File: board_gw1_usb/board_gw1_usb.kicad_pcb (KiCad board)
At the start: 4 copper layers, 50 x 15.2 mm, 212 parts, among them J1 USB_C_Receptacle, Q1 2N7002, Q10 2N7002, Q11 2N7002, Q12 2N7002, Q13 2N7002, Q14 2N7002, Q15 2N7002, Q16 2N7002, Q17 2N7002, Q18 2N7002, Q19 2N7002, Q2 2N7002, Q20 2N7002, Q21 2N7002, Q22 2N7002, Q23 2N7002, Q24 2N7002, Q25 2N7002, Q26 2N7002, Q27 2N7002, Q28 2N7002, Q29 2N7002, Q3 2N7002, Q30 2N7002, Q31 2N7002, Q32 2N7002, Q33 2N7002, Q34 2N7002, Q35 2N7002, Q36 2N7002, Q37 2N7002, Q38 2N7002, Q39 2N7002, Q4 2N7002, Q40 2N7002, Q41 2N7002, Q5 2N7002, Q6 2N7002, Q7 2N7002, Q8 2N7002, Q9 2N7002, U1 GW1NR-LV9-QN88-C6/I5, U11 FT232H, U2 ESD224DQA, U3 MIC5203-3.3BM5, U4 APS6404L-3SQR-ZR, U5 MIC5504-1.2YM5, U6 AP62150Z6, U7 W25Q16JVUXIQ, X1 27MHz

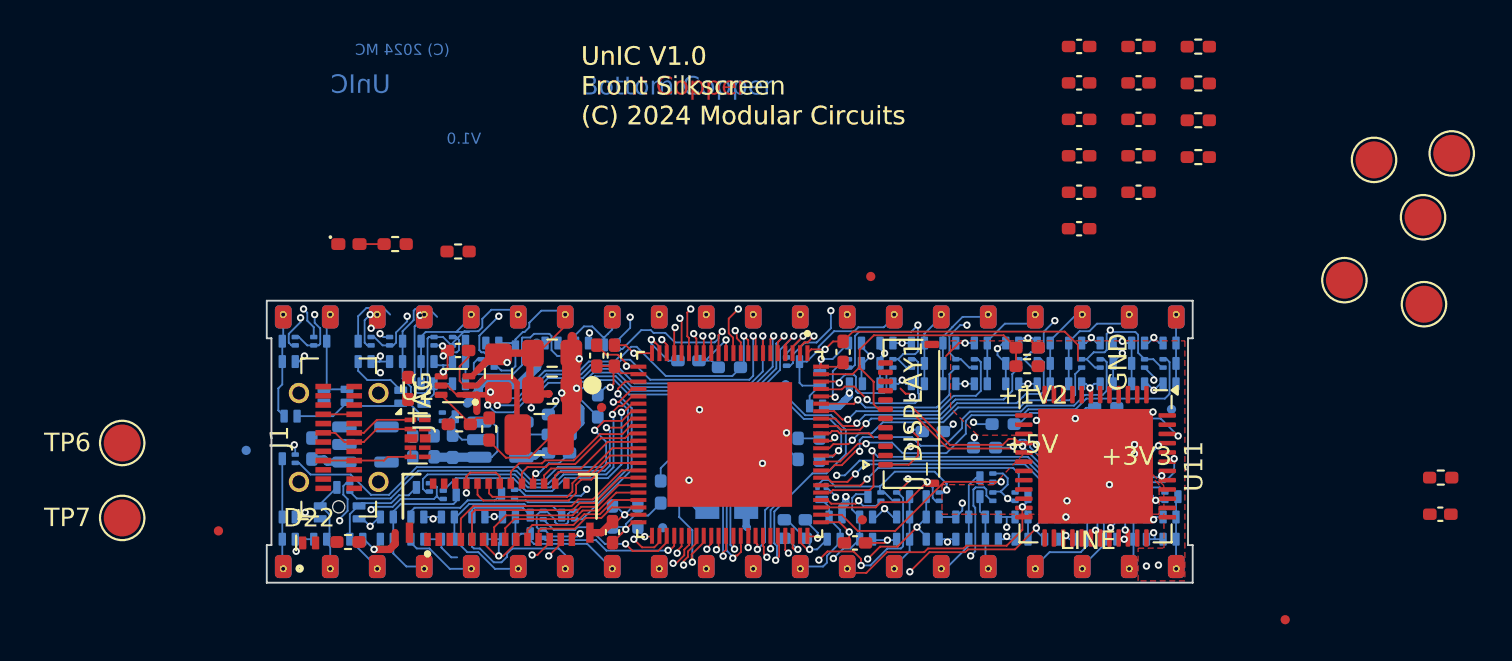
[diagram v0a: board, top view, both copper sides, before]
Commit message: Integrated JTAG controller mostly routed.
There are still some keepout violations and power nets
are incomplete, but at least there's a light at the end
if the tunnel.
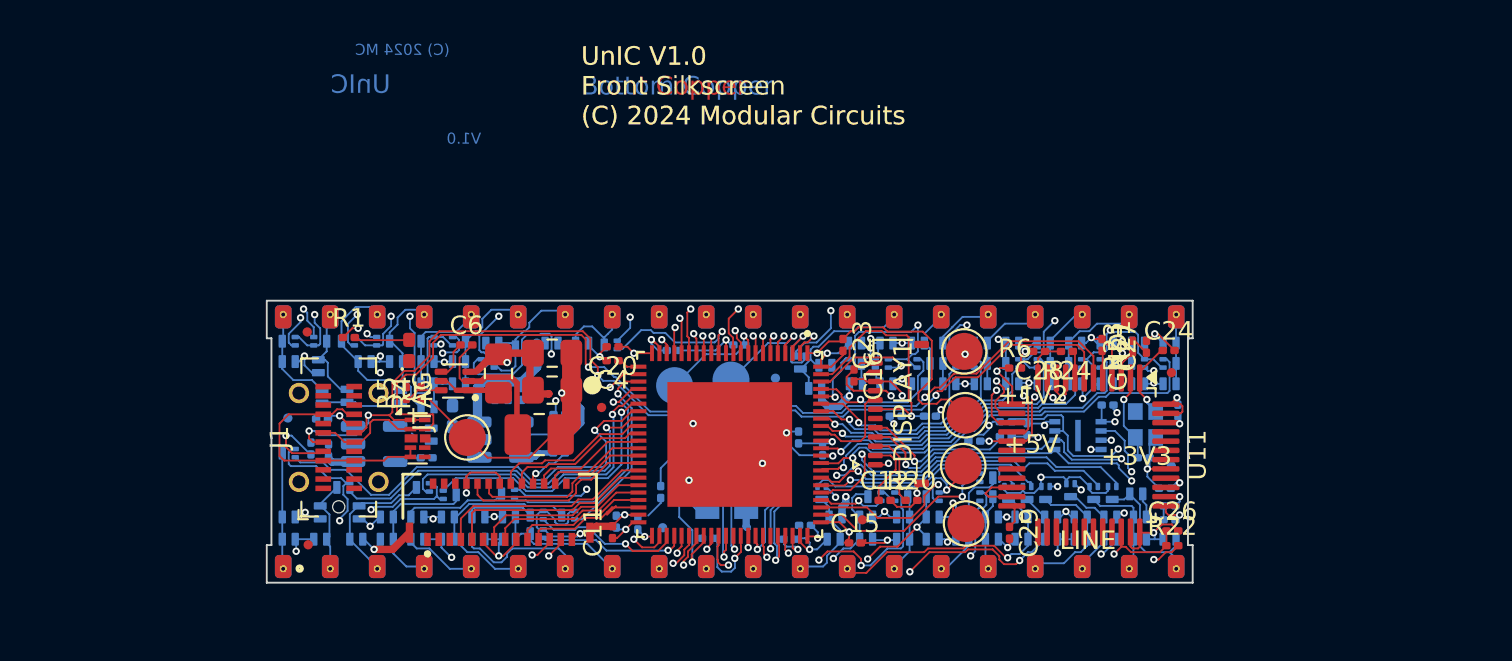
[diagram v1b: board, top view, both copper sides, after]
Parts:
- removed C32: 2.2u, UNIC:C_0402_1005Metric_Pad0.74x0.62mm_HandSolder
- added Y1: 12MHz, Crystal:Crystal_SMD_2016-4Pin_2.0x1.6mm, B.Cu at (85.8, 61.8)
- C1: footprint UNIC:C_0402_1005Metric_Pad0.74x0.62mm_HandSolder -> Capacitor_SMD:C_0402_1005Metric_Pad0.74x0.62mm_HandSolder
- C10, C11, C12, C13, C14, C15, C17, C18, C19, C2, C20, C21, C22, C23, C24, C26, C27, C28, C29, C3, C4, C6, C9: footprint UNIC:C_0402_1005Metric_Pad0.74x0.62mm_HandSolder -> Capacitor_SMD:C_0201_0603Metric
- C16: footprint UNIC:C_0402_1005Metric_Pad0.74x0.62mm_HandSolder -> Capacitor_SMD:C_0201_0603Metric; moved to F.Cu
- C25, C30, C31, C33, C34: footprint UNIC:C_0402_1005Metric_Pad0.74x0.62mm_HandSolder -> Capacitor_SMD:C_0201_0603Metric; moved to B.Cu
- D22, TP6, TP7: moved to B.Cu
- R1, R10, R11, R12, R13, R14, R15, R17, R20, R21, R22, R23, R24, R4, R5, R7, R8, R9: footprint UNIC:R_0402_1005Metric_Pad0.72x0.64mm_HandSolder -> Resistor_SMD:R_0201_0603Metric
- R16, R18, R19, R2, R3: footprint UNIC:R_0402_1005Metric_Pad0.72x0.64mm_HandSolder -> Resistor_SMD:R_0201_0603Metric; moved to B.Cu
- R6: footprint UNIC:R_0402_1005Metric_Pad0.72x0.64mm_HandSolder -> Resistor_SMD:R_0201_0603Metric; moved to F.Cu
- U11: footprint Package_DFN_QFN:QFN-48-1EP_8x8mm_P0.5mm_EP6.2x6.2mm -> Package_QFP:LQFP-48_7x7mm_P0.5mm
- moved TP3 53.0 mm to (49.1, 62.5)
- moved FID2 33.7 mm to (40.5, 68.3)
- moved TP6 33.1 mm to (63.4, 59.4), turned to 180 degrees
- moved TP7 30.7 mm to (60.3, 59.7), turned to 180 degrees
- moved C12 30.0 mm to (71.7, 65.9)
- moved R16 29.7 mm to (76.5, 62.7)
- moved R20 28.6 mm to (73.1, 65.9)
- moved TP5 28.4 mm to (76.0, 57.8)
- moved TP1 27.4 mm to (76.1, 67.1)
- moved TP4 26.1 mm to (76.0, 61.3)
- moved R22 25.0 mm to (87.2, 68.3)
- moved TP2 22.9 mm to (75.9, 64.0)
- moved C26 22.8 mm to (87.2, 67.5)
- moved R6 22.6 mm to (78.7, 58.7), turned to 0 degrees
- moved C31 22.0 mm to (86.8, 65.2), turned to 180 degrees
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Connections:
- J_EXT1 pad 1: /JTAG_SEL_N -> unconnected-(J_EXT1-Pin_1-Pad1)
- J_EXT1 pad 2: /JTAG_TDI -> unconnected-(J_EXT1-Pin_2-Pad2)
- J_EXT1 pad 3: /RECONFIG_N -> unconnected-(J_EXT1-Pin_3-Pad3)
- J_EXT1 pad 4: /JTAG_TDO -> unconnected-(J_EXT1-Pin_4-Pad4)
- J_EXT1 pad 5: /JTAG_TMS -> unconnected-(J_EXT1-Pin_5-Pad5)
- J_EXT1 pad 6: /JTAG_TCK -> unconnected-(J_EXT1-Pin_6-Pad6)
- U11 pad 18: /RECONFIG_N -> unconnected-(U11-ADBUS5-Pad18)
- U11 pad 19: /DONE -> unconnected-(U11-ADBUS6-Pad19)
- U2 pad 10: unconnected-(U2-Pad10) -> /USB_DP
- U2 pad 9: unconnected-(U2-Pad9) -> /USB_DM
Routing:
- net /USB_DP: track 3.33 -> 57.0 mm, vias 0 -> 4
- net /USB_DM: track 5.21 -> 56.5 mm, vias 0 -> 2
- net GND: track 85.7 -> 112.3 mm, vias 40 -> 44
- net /RECONFIG_N: track 18.5 -> 6.28 mm, vias 2 -> 1
- net /JTAG_SEL_N: track 14.1 -> 26.2 mm, vias 2 -> 3
- net +3V3: track 48.8 -> 60.1 mm, vias 15 -> 17
- net /SPI_MISO_IO1: track 53.5 -> 44.0 mm
- net /SPI_IO3: track 49.7 -> 40.8 mm
- net /SPI_MOSI_IO0: track 55.2 -> 47.8 mm
- net /VBUS: track 6.96 -> 14.0 mm
- net /SPI_IO2: track 47.1 -> 40.2 mm
- net +5V: track 93.2 -> 99.6 mm, vias 21 -> 17
- net /FLASH_CS_N: track 36.5 -> 30.3 mm
- net LINE: track 48.7 -> 42.8 mm
- net /SPI_CLK: track 53.9 -> 48.5 mm
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- removed copper zone on F.Cu, net +3V3
- removed copper zone on F.Cu, net +5V

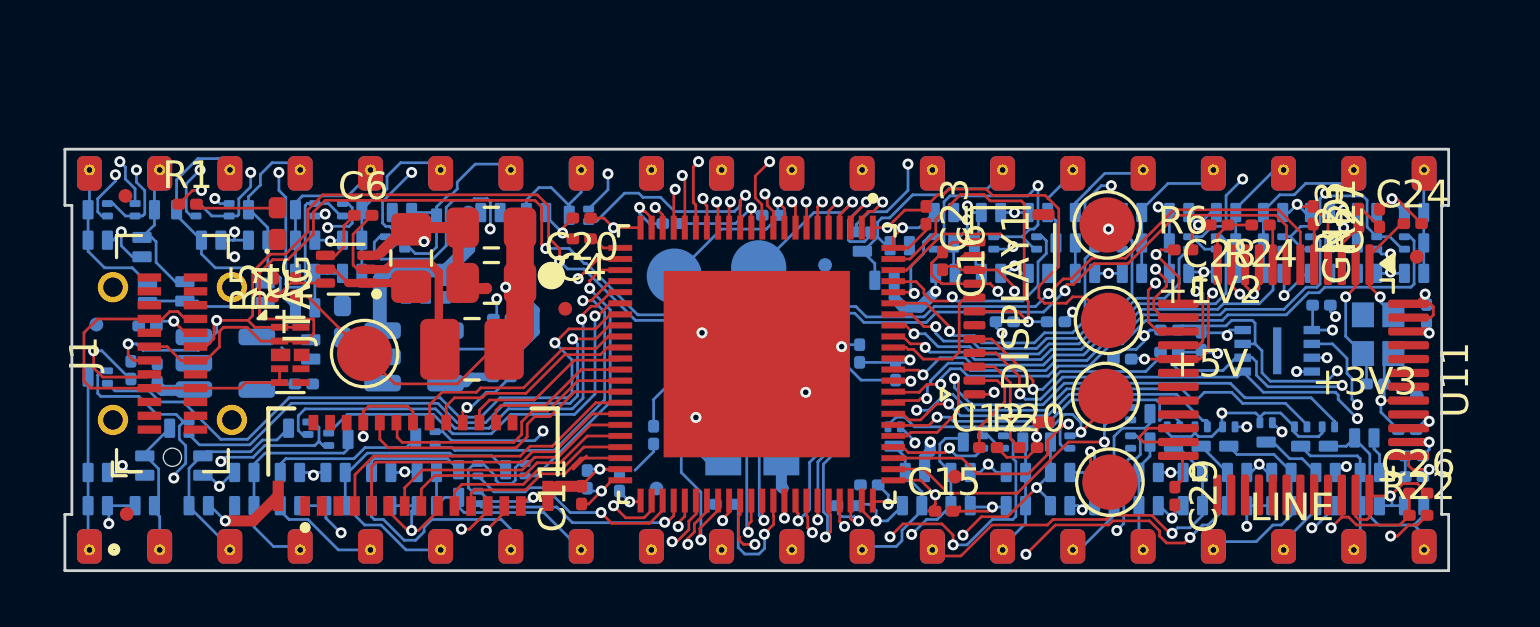
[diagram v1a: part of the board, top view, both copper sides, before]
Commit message: UnIC with FT232H is fully routed.
Not all that nicely, power needs a lot more work. But at least
connectivity is there.
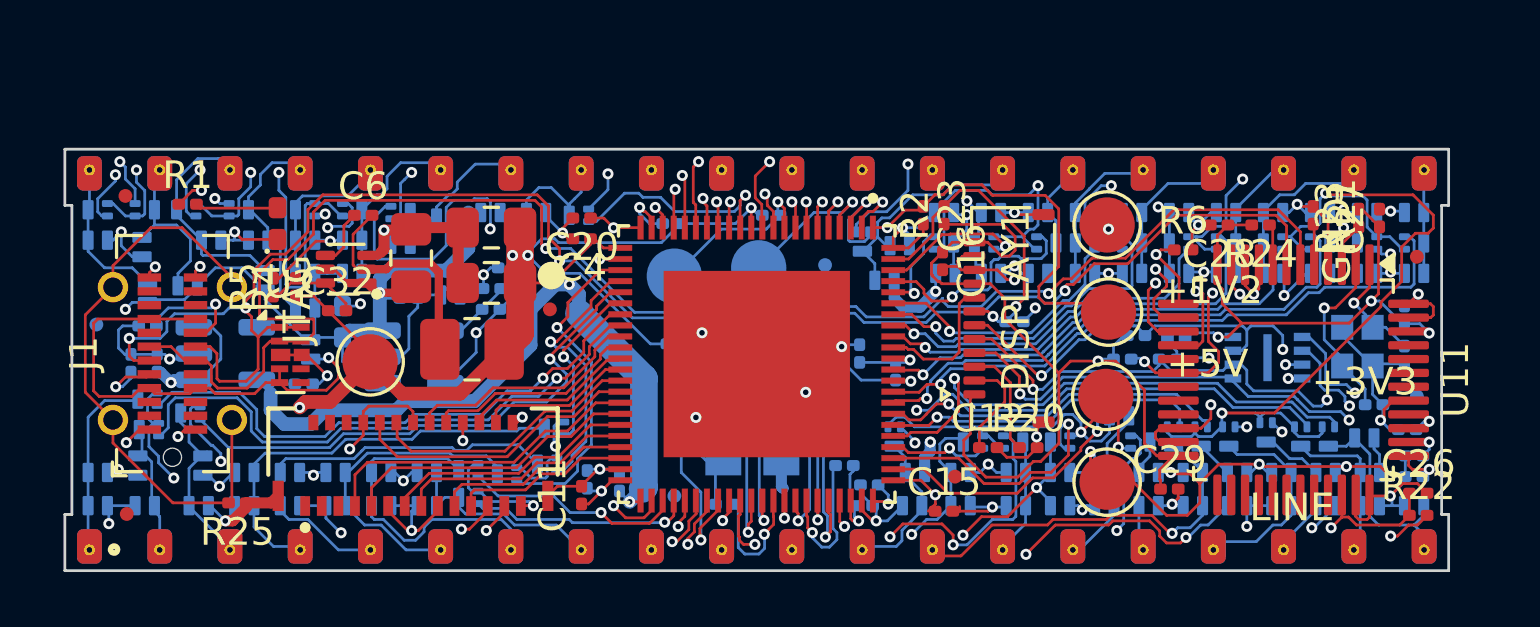
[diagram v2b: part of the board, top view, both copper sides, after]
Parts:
- added C32: 33p, Capacitor_SMD:C_0201_0603Metric, F.Cu at (48.1, 60.9)
- added R25: 0, Resistor_SMD:R_0201_0603Metric, F.Cu at (44.5, 67.9)
- C24: moved to B.Cu
- R2: moved to F.Cu
- U6: value AP62150Z6 -> TPS562242
- Y1: footprint Crystal:Crystal_SMD_2016-4Pin_2.0x1.6mm -> UNIC:Crystal_SMD_2016-4Pin_2.0x1.6mm
- moved R8 18.2 mm to (66.5, 66.5)
- moved Q2 7.81 mm to (56.0, 65.2), turned to 180 degrees
- moved C24 4.76 mm to (86.7, 62.5), turned to -90 degrees
- moved Q8 4.50 mm to (55.7, 66.5)
- moved R2 4.43 mm to (70.1, 57.5), turned to 90 degrees
- moved C3 3.94 mm to (54.3, 59.4), turned to 180 degrees
- moved Q3 3.94 mm to (42.8, 64.6)
- moved R9 3.40 mm to (60.4, 62.1), turned to 0 degrees
- moved Q1 1.97 mm to (41.3, 64.1)
- moved R3 1.50 mm to (72.6, 61.3)
- moved R14 1.49 mm to (53.7, 60.9)
- moved R17 1.39 mm to (50.7, 60.5), turned to 0 degrees
- moved Q41 1.25 mm to (52.2, 60.4), turned to 180 degrees
- moved R10 1.22 mm to (77.0, 61.8)
- moved R15 1.17 mm to (53.7, 60.1)
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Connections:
- J1 pad S1: GND -> Net-(J1-SHIELD)
- J_DISPLAY1 pad 6: /SPI_IO2 -> /SPI_IO3
- U11 pad 17: /JTAG_SEL_N -> unconnected-(U11-ADBUS4-Pad17)
- U11 pad 18: unconnected-(U11-ADBUS5-Pad18) -> /JTAG_SEL_N
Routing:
- net +3V3: track 60.1 -> 201.1 mm, vias 17 -> 18
- net LINE: track 42.8 -> 154.8 mm, vias 17 -> 19
- net +5V: track 99.6 -> 197.6 mm, vias 17 -> 18
- net +1V2: track 40.7 -> 67.8 mm, vias 4 -> 5
- net Net-(J1-SHIELD): track 0.00 -> 22.4 mm
- net GND: track 112.3 -> 128.8 mm, vias 44 -> 52
- net /SPI_IO3: track 40.8 -> 49.4 mm, vias 2 -> 3
- net /PIN4_F: track 14.7 -> 6.22 mm
- net /PIN4: track 8.21 -> 15.3 mm
- net Net-(Q41-D): track 0.00 -> 4.71 mm
- net /PIN5: track 10.8 -> 15.5 mm
- net /USB_DP: track 57.0 -> 61.1 mm
- net /VBUS: track 14.0 -> 18.0 mm, vias 0 -> 1
- net /PIN1_F: track 23.4 -> 19.7 mm
- net /FLASH_CS_N: track 30.3 -> 33.7 mm
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- removed copper zone on In2.Cu, net +1V2
- removed copper zone on In1.Cu, net +3V3
- removed copper zone on In2.Cu, net +3V3
- removed copper zone on In1.Cu, net +5V
- removed copper zone on In2.Cu, net +5V
- removed copper zone on In2.Cu, net LINE

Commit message: UnIC wuth ISB (V2.0) is pretty much complete.
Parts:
- C29: moved to B.Cu
- moved C29 3.24 mm to (78.7, 64.2)
- moved Q35 2.40 mm to (52.8, 57.3), turned to 180 degrees
- moved C3 2.16 mm to (54.1, 61.5), turned to 90 degrees
- moved D65 1.80 mm to (50.3, 57.6), turned to 90 degrees
- moved FID8 1.59 mm to (56.9, 59.7)
- moved D66 1.45 mm to (51.5, 57.6), turned to -90 degrees
- moved Q36 1.32 mm to (58.2, 57.3)
- moved D68 1.30 mm to (56.6, 57.4)
- moved D67 1.30 mm to (55.0, 57.4)
- moved FID6 0.91 mm to (87.3, 58.1)
- moved Q33 0.75 mm to (46.2, 57.3), turned to 0 degrees
- moved R14 0.72 mm to (53.4, 61.5), turned to 90 degrees
- moved Q13 0.63 mm to (75.8, 64.7), turned to 180 degrees
- moved C6 0.45 mm to (49.1, 57.9)
- moved R6 0.38 mm to (78.6, 58.4)
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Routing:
- net /PIN34_F: track 19.7 -> 11.1 mm
- net +5V: track 197.6 -> 191.0 mm, vias 18 -> 20
- net LINE: track 154.8 -> 148.4 mm, vias 19 -> 20
- net +3V3: track 201.1 -> 206.6 mm, vias 18 -> 19
- net /LCD_RST_N: track 11.5 -> 13.9 mm
- net /PIN36_F: track 16.5 -> 18.6 mm
- net /PIN33_F: track 7.98 -> 6.47 mm
- net /PIN29: track 14.4 -> 15.8 mm
- net /PIN33: track 5.72 -> 4.45 mm
- net /JTAG_TDO: track 18.2 -> 19.3 mm
- net GND: track 128.8 -> 129.9 mm, vias 52 -> 53
- net /PIN35_F: track 17.8 -> 16.7 mm
- net Net-(J1-SHIELD): track 22.4 -> 23.5 mm
- net /PIN36: track 5.70 -> 6.75 mm
- net /PIN3_F: track 19.1 -> 20.0 mm
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- added copper zone on F.Cu, net +3V3
- added copper zone on In1.Cu, net +3V3
- added copper zone on In2.Cu, net +3V3
- added copper zone on In1.Cu, net +5V
- added copper zone on In2.Cu, net GND
- added copper zone on F.Cu, net LINE
- added copper zone on In2.Cu, net LINE
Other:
- board text added: "(C) 2025"
- board text added: "Modular Circuits"
- board text added: "UnIC V2.0 Bottom Copper (C) 2025 Modular Circuits"
- board text added: "UnIC V2.0 Bottom Fab Drawing (C) 2025 Modular Circuits"
- board text added: "UnIC V2.0 Bottom Mask (C) 2025 Modular Circuits"
- board text added: "UnIC V2.0 Bottom Paste (C) 2025 Modular Circuits"
- board text added: "UnIC V2.0 Bottom Silkscreen (C) 2025 Modular Circuits"
- board text added: "UnIC V2.0 Front Copper (C) 2025 Modular Circuits"
- board text added: "UnIC V2.0 Front Fab Drawing (C) 2025 Modular Circuits"
- board text added: "UnIC V2.0 Front Mask (C) 2025 Modular Circuits"
- board text added: "UnIC V2.0 Front Paste (C) 2025 Modular Circuits"
- board text added: "UnIC V2.0 Front Silkscreen (C) 2025 Modular Circuits"
- board text added: "UnIC V2.0 Layer 2 Copper (C) 2025 Modular Circuits"
- board text added: "UnIC V2.0 Layer 3 Copper (C) 2025 Modular Circuits"
- board text added: "V2.0"
- board text added: "~{JTAG_SEL}"
- board text added: "~{RECONFIG}"
- board text removed: "(C) 2024 MC"
- board text removed: "JTAG"
- board text removed: "UnIC V1.0 Bottom Copper (C) 2024 Modular Circuits"
- board text removed: "UnIC V1.0 Bottom Fab Drawing (C) 2024 Modular Circuits"
- board text removed: "UnIC V1.0 Bottom Mask (C) 2024 Modular Circuits"
- board text removed: "UnIC V1.0 Bottom Paste (C) 2024 Modular Circuits"
- board text removed: "UnIC V1.0 Front Copper (C) 2024 Modular Circuits"
- board text removed: "UnIC V1.0 Front Fab Drawing (C) 2024 Modular Circuits"
- board text removed: "UnIC V1.0 Front Mask (C) 2024 Modular Circuits"
- board text removed: "UnIC V1.0 Front Paste (C) 2024 Modular Circuits"
- board text removed: "UnIC V1.0 Front Silkscreen (C) 2024 Modular Circuits"
- board text removed: "UnIC V1.0 Layer 2 Copper (C) 2024 Modular Circuits"
- board text removed: "UnIC V1.0 Layer 3 Copper (C) 2024 Modular Circuits"
- board text removed: "V1.0"
